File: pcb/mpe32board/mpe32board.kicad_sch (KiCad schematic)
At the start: 37 parts, among them J1 Conn_ST_STDC14, J2 USB_C_Receptacle_USB2.0_16P, SW1 SW_Push, SW2 SW_Push, U10 W9812G6KH-75, U2 USBLC6-2P6, U3 AMS1117-3.3, U9 STM32H743IITx

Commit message: codec
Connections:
- net NEOPIXEL_IN: now also U9.47 (PA3)
- net SDMMC1_D0: now reaches U9.117 (PC8)
- net SDMMC1_D2: now reaches U9.139 (PC10)
- net SDMMC1_D3: now reaches U9.140 (PC11)
- net SDMMC1_CK: now reaches U9.141 (PC12)
- net SDMMC1_CMD: now reaches U9.144 (PD2)
- net I2C2_SCL: now reaches U9.45 (PH4)
- net I2C2_SDA: now reaches U9.46 (PH5)
- net I2S1_WS: now reaches U9.50 (PA4)
- net I2S1_CK: now reaches U9.51 (PA5)
- net I2S1_SDI: now reaches U9.52 (PA6)
- net I2S1_SDO: now reaches U9.53 (PA7)
- net I2C4_SCL: now reaches U9.88 (PH11)
- net I2C4_SDA: now reaches U9.89 (PH12)
- net TAC5212_GPO1: now reaches U9.92 (PB12)
- net TAC5212_GPI1: now reaches U9.93 (PB13)
- net SCL_0 renamed I2C1_SCL
- net SCL_1: no longer names the net of U9.167 (PB8)
- net SCL_2 renamed TAC5212_GPIO1
- net SCL_3: no longer names the net of U9.119 (PA8)
- net SDA_0 renamed I2C1_SDA
- net SDA_1: no longer names the net of U9.168 (PB9)
- net SDA_2 renamed TAC5212_GPIO2
- net SDA_3 renamed SDMMC1_D1
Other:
- added sheet 16x2-4 LCD Display (lcddisplay.kicad_sch)
- added sheet Audio Codec (audioic.kicad_sch)
- added sheet MicroSD Card (microsd.kicad_sch)
- note added: "extra for IIT"
- note added: "i2c1"
- note added: "i2c2"
- note added: "i2c4"

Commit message: layout stuff
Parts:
- added J46: Conn_02x10_Counter_Clockwise, Connector_PinHeader_2.54mm:PinHeader_2x10_P2.54mm_Vertical, symbol Connector_Generic:Conn_02x10_Counter_Clockwise
- C1, C10, C11, C12, C13, C14, C15, C16, C17, C18, C19, C2, C20, C21, C22, C23, C24, C25, C3, C4, C5, C6, C7, C8, C9: footprint (none) -> Capacitor_SMD:C_0603_1608Metric
- J2: footprint (none) -> Connector_USB:USB_C_Receptacle_GCT_USB4105-xx-A_16P_TopMnt_Horizontal
- R1, R2, R3, R4: footprint (none) -> Resistor_SMD:R_0603_1608Metric
- SW1, SW2: footprint (none) -> Button_Switch_THT:SW_PUSH_6mm
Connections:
- net NEOPIXEL_INTERNAL: now reaches U9.42 (PA2)
- net SWO renamed JTDO
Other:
- added sheet Control Debug Keys and Internal Neopixels (debugdispcontrol.kicad_sch)
- note added: "only uses serial wire or jtag (serial wire priority)"
- note added: "sdmmc1"

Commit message: board layout stuff
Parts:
- added H1, H2, H3, H4: MountingHole_Pad, MountingHole:MountingHole_3.2mm_M3_DIN965_Pad, symbol Mechanical:MountingHole_Pad
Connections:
- net BTN1_INTERNAL: now also U9.175 (PI6)
- net BTN2_INTERNAL: now also U9.174 (PI5)
- net BTN3_INTERNAL: now also U9.173 (PI4)
- net BTN4_INTERNAL: now also U9.134 (PI3)
- net GND: now also H1.1, H2.1, H3.1, H4.1
- net SDCARD_DET: now reaches U9.41 (PA1)

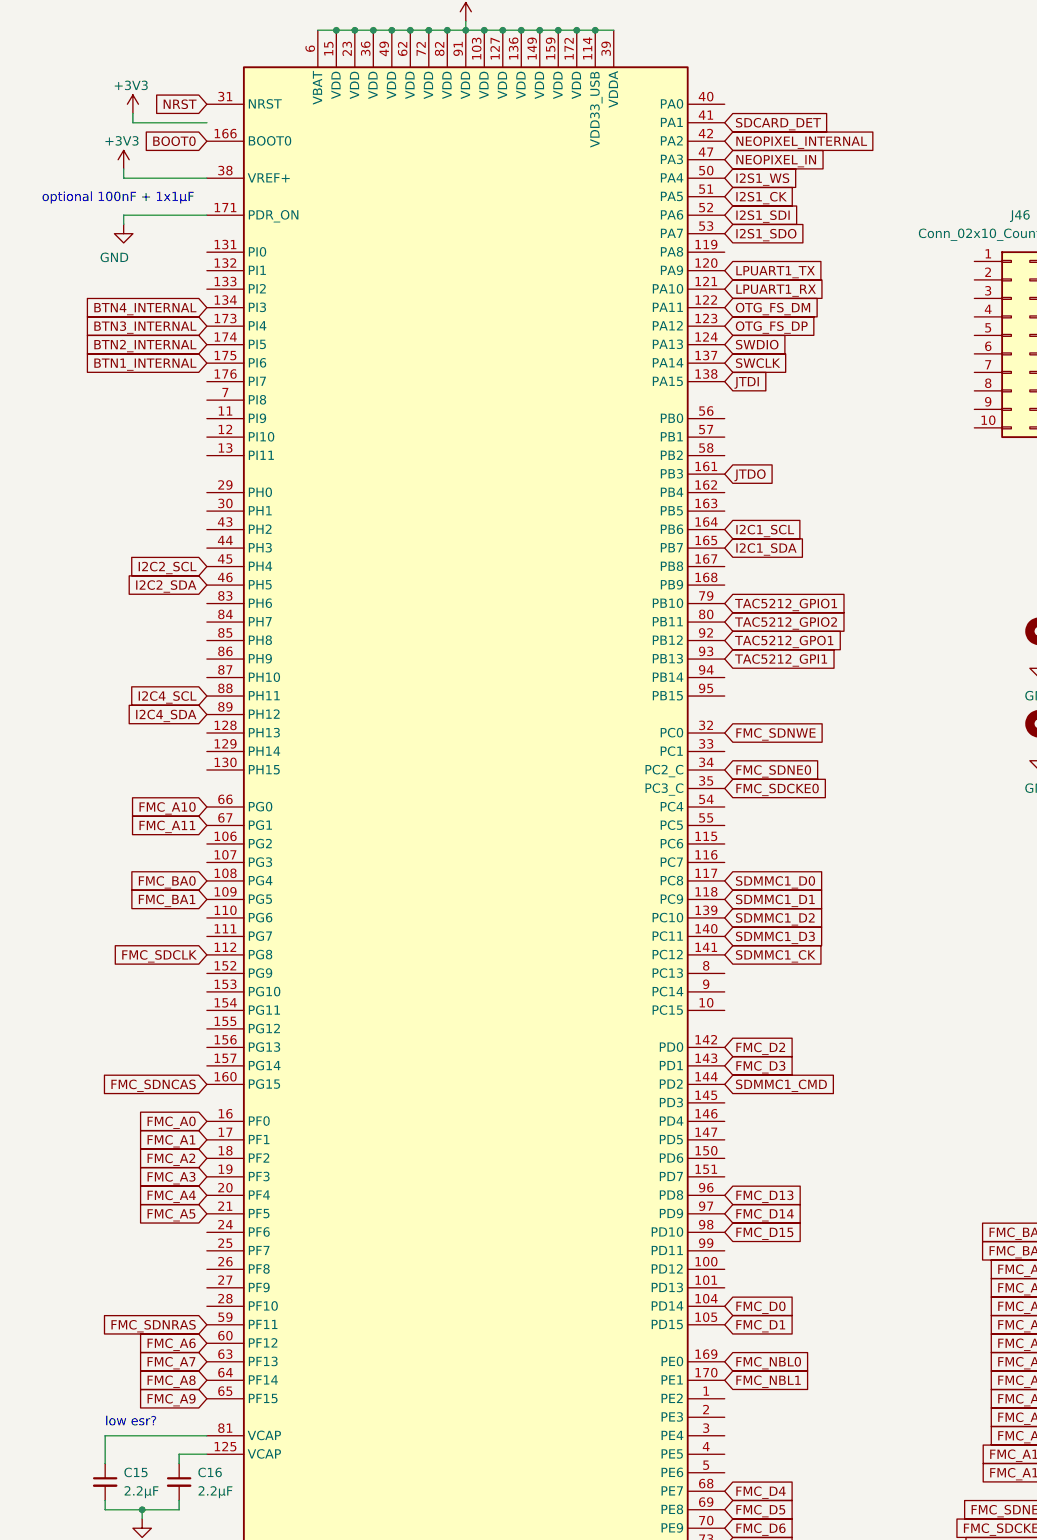
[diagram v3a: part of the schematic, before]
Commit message: routed data bus of ram
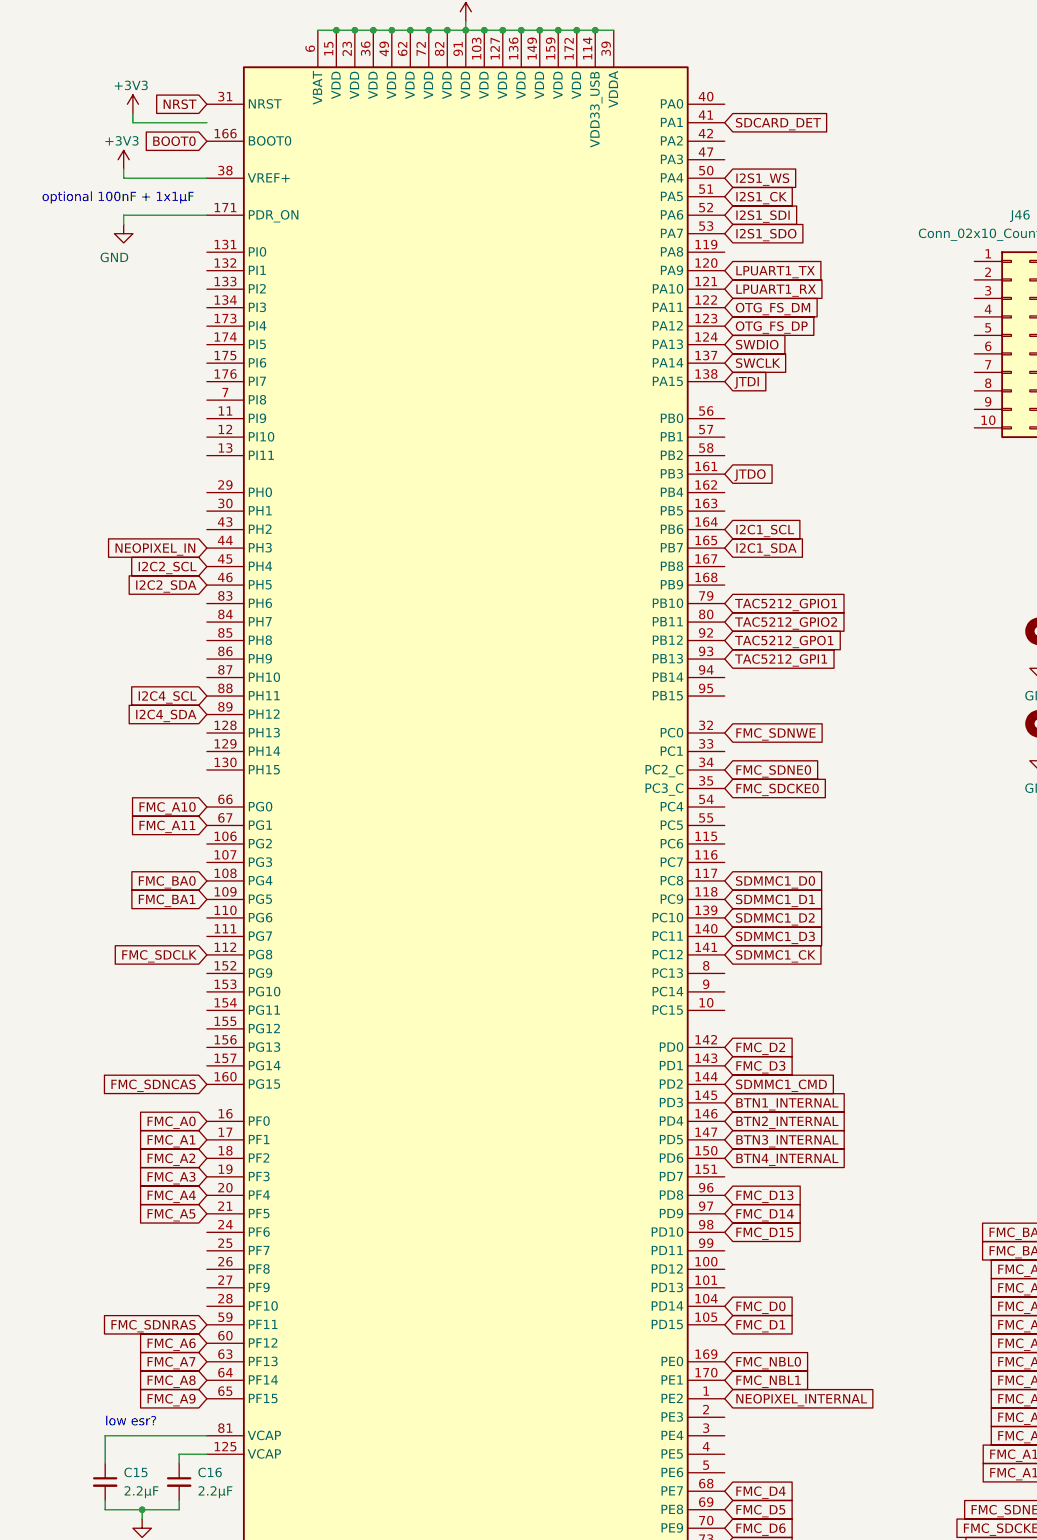
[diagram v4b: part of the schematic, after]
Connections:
- net BTN1_INTERNAL: now also U9.145 (PD3); no longer U9.175 (PI6)
- net BTN2_INTERNAL: now also U9.146 (PD4); no longer U9.174 (PI5)
- net BTN3_INTERNAL: now also U9.147 (PD5); no longer U9.173 (PI4)
- net BTN4_INTERNAL: now also U9.150 (PD6); no longer U9.134 (PI3)
- net NEOPIXEL_IN: now also U9.44 (PH3); no longer U9.47 (PA3)
- net NEOPIXEL_INTERNAL: now also U9.1 (PE2); no longer U9.42 (PA2)

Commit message: routed ram
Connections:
- net TAC5212_GPI1: now also U9.40 (PA0); no longer U9.93 (PB13)
- net TAC5212_GPO1: now also U9.42 (PA2); no longer U9.92 (PB12)
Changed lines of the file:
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@@
 		)
 	)
-	(text "i2c4"
+	(text "i2c2\n"
 		(exclude_from_sim no)
 		(at 332.994 223.774 0)
@@
 		)
 	)
-	(text "i2c1"
+	(text "i2c4"
 		(exclude_from_sim no)
 		(at 358.2199 194.2105 0)
@@
 		)
 	)
-	(text "i2c2"
+	(text "i2c1"
 		(exclude_from_sim no)
 		(at 254.762 201.168 0)
@@
 		)
 	)
-	(global_label "FMC_D6"
+	(global_label "TAC5212_GPI1"
 		(shape input)
-		(at 111.76 237.49 0)
+		(at 111.76 41.91 0)
 		(fields_autoplaced yes)
 		(effects
@@
 		)
 		(property "Intersheetrefs" "${INTERSHEET_REFS}"
-			(at 122.0023 237.49 0)
+			(at 128.2313 41.91 0)
 			(hide yes)
 			(show_name no)
@@
 		)
 	)
-	(global_label "FMC_SDNCAS"
+	(global_label "FMC_D6"
 		(shape input)
-		(at 40.64 176.53 180)
+		(at 111.76 237.49 0)
 		(fields_autoplaced yes)
 		(effects
@@
 				(size 1.27 1.27)
 			)
-			(justify right)
+			(justify left)
 		)
 		(property "Intersheetrefs" "${INTERSHEET_REFS}"
-			(at 25.4991 176.53 0)
+			(at 122.0023 237.49 0)
 			(hide yes)
 			(show_name no)
@@
 					(size 1.27 1.27)
 				)
-				(justify right)
+				(justify left)
 			)
 		)
 	)
-	(global_label "NRST"
+	(global_label "FMC_SDNCAS"
 		(shape input)
-		(at 40.64 41.91 180)
+		(at 40.64 176.53 180)
 		(fields_autoplaced yes)
 		(effects
@@
 		)
 		(property "Intersheetrefs" "${INTERSHEET_REFS}"
-			(at 32.8772 41.91 0)
+			(at 25.4991 176.53 0)
 			(hide yes)
 			(show_name no)
@@
 		)
 	)
-	(global_label "TAC5212_GPI1"
+	(global_label "NRST"
 		(shape input)
-		(at 111.76 118.11 0)
+		(at 40.64 41.91 180)
 		(fields_autoplaced yes)
 		(effects
@@
 				(size 1.27 1.27)
 			)
-			(justify left)
+			(justify right)
 		)
 		(property "Intersheetrefs" "${INTERSHEET_REFS}"
-			(at 128.2313 118.11 0)
+			(at 32.8772 41.91 0)
 			(hide yes)
 			(show_name no)
@@
 					(size 1.27 1.27)
 				)
-				(justify left)
+				(justify right)
 			)
 		)
@@
 		)
 	)
-	(global_label "BTN3_INTERNAL"
+	(global_label "TAC5212_GPO1"
 		(shape input)
-		(at 111.76 184.15 0)
+		(at 111.76 46.99 0)
 		(fields_autoplaced yes)
 		(effects
@@
 		)
 		(property "Intersheetrefs" "${INTERSHEET_REFS}"
-			(at 129.2595 184.15 0)
+			(at 128.957 46.99 0)
 			(hide yes)
 			(show_name no)
@@
 		)
 	)
-	(global_label "BTN1_INTERNAL"
+	(global_label "BTN3_INTERNAL"
 		(shape input)
-		(at 111.76 179.07 0)
+		(at 111.76 184.15 0)
 		(fields_autoplaced yes)
 		(effects
@@
 		)
 		(property "Intersheetrefs" "${INTERSHEET_REFS}"
-			(at 129.2595 179.07 0)
+			(at 129.2595 184.15 0)
 			(hide yes)
 			(show_name no)
@@
 		)
 	)
-	(global_label "FMC_SDNWE"
+	(global_label "BTN1_INTERNAL"
 		(shape input)
-		(at 111.76 128.27 0)
+		(at 111.76 179.07 0)
 		(fields_autoplaced yes)
 		(effects
@@
 		)
 		(property "Intersheetrefs" "${INTERSHEET_REFS}"
-			(at 125.9332 128.27 0)
+			(at 129.2595 179.07 0)
 			(hide yes)
 			(show_name no)
@@
 		)
 	)
-	(global_label "FMC_D9"
+	(global_label "FMC_SDNWE"
 		(shape input)
-		(at 111.76 245.11 0)
+		(at 111.76 128.27 0)
 		(fields_autoplaced yes)
 		(effects
@@
 		)
 		(property "Intersheetrefs" "${INTERSHEET_REFS}"
-			(at 122.0023 245.11 0)
+			(at 125.9332 128.27 0)
 			(hide yes)
 			(show_name no)
@@
 		)
 	)
-	(global_label "TAC5212_GPO1"
+	(global_label "FMC_D9"
 		(shape input)
-		(at 111.76 115.57 0)
+		(at 111.76 245.11 0)
 		(fields_autoplaced yes)
 		(effects
@@
 		)
 		(property "Intersheetrefs" "${INTERSHEET_REFS}"
-			(at 128.957 115.57 0)
+			(at 122.0023 245.11 0)
 			(hide yes)
 			(show_name no)

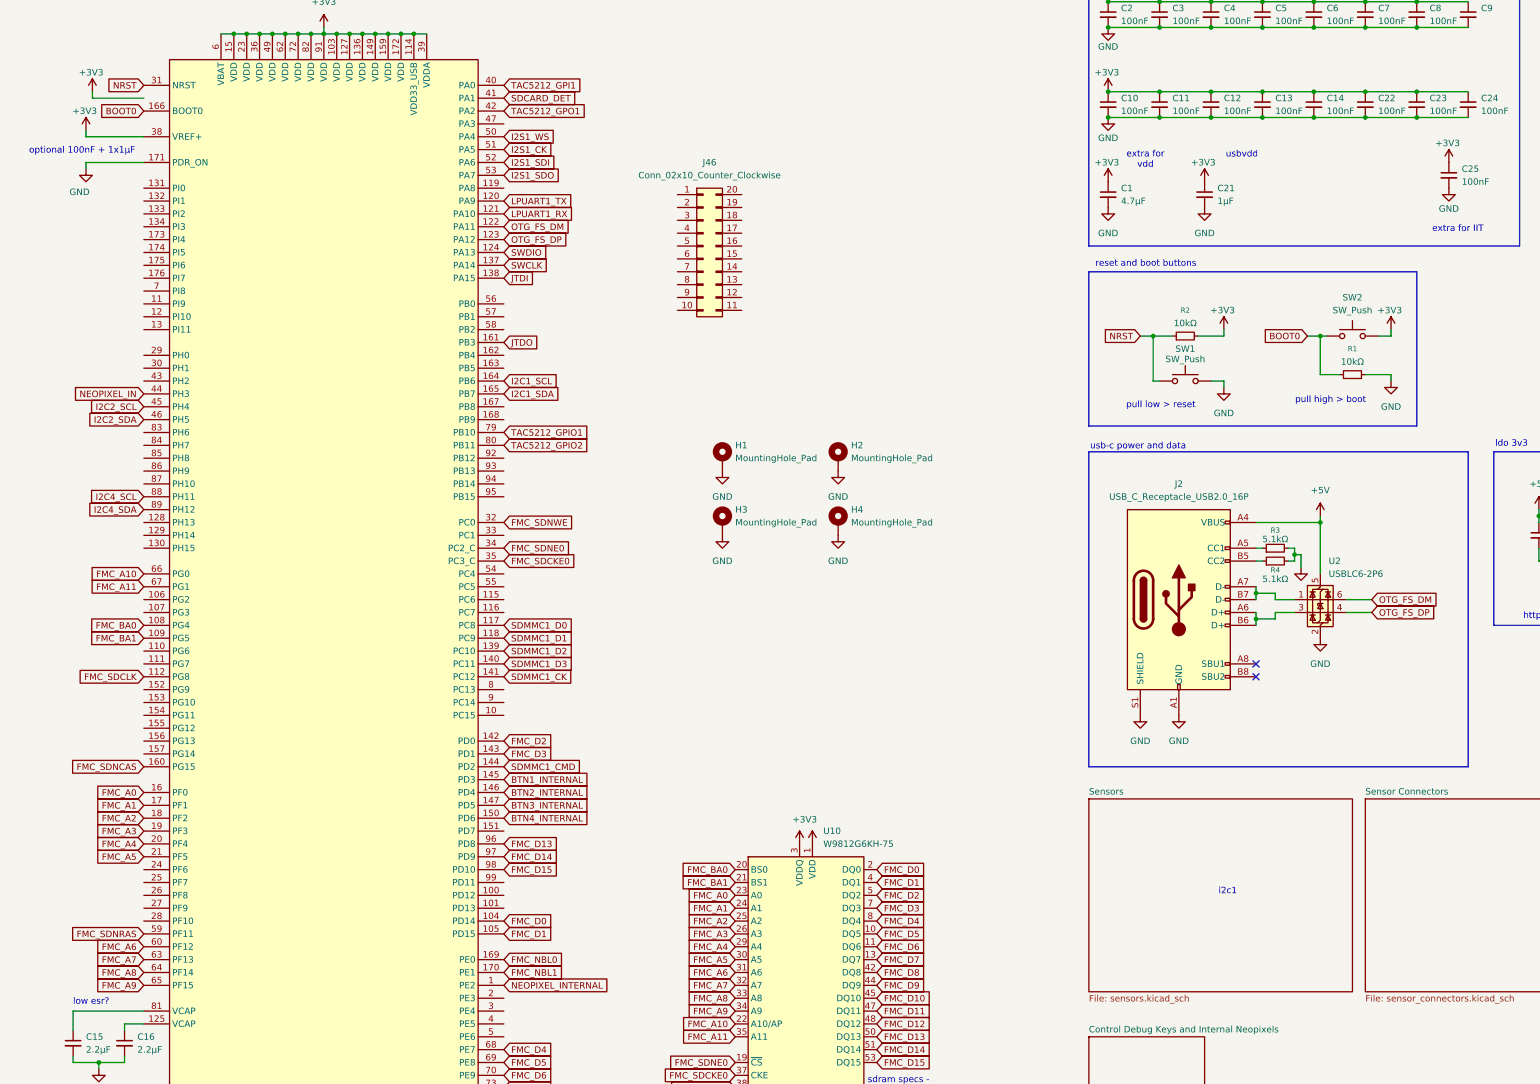
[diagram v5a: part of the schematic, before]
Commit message: routed audio codec and sdram
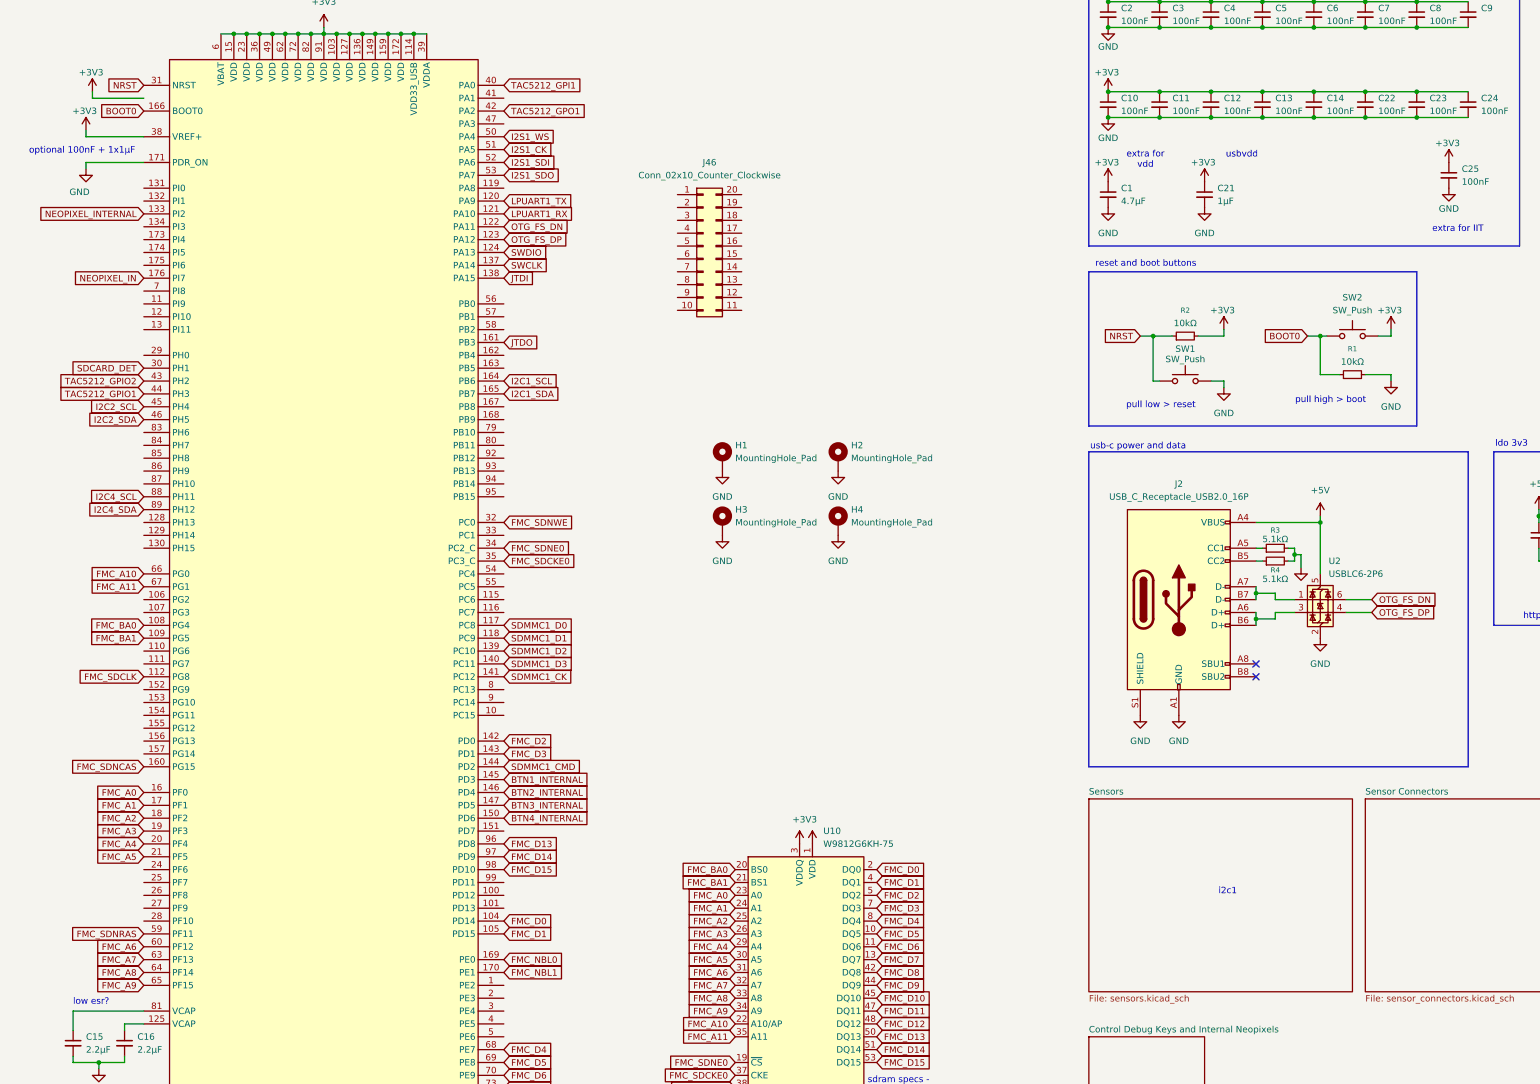
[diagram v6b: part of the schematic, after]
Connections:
- net NEOPIXEL_IN: now also U9.176 (PI7); no longer U9.44 (PH3)
- net NEOPIXEL_INTERNAL: now also U9.133 (PI2); no longer U9.1 (PE2)
- net SDCARD_DET: now also U9.30 (PH1); no longer U9.41 (PA1)
- net TAC5212_GPIO1: now also U9.44 (PH3); no longer U9.79 (PB10)
- net TAC5212_GPIO2: now also U9.43 (PH2); no longer U9.80 (PB11)
- net OTG_FS_DM renamed OTG_FS_DN

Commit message: route connectors
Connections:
- net BTN1_INTERNAL: now also U9.99 (PD11); no longer U9.145 (PD3)
- net BTN2_INTERNAL: now also U9.100 (PD12); no longer U9.146 (PD4)
- net BTN3_INTERNAL: now also U9.116 (PC7); no longer U9.147 (PD5)
- net BTN4_INTERNAL: now also U9.119 (PA8); no longer U9.150 (PD6)
- net RESET_0: now reaches U9.134 (PI3)
